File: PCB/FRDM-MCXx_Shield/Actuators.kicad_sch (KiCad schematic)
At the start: 20 parts, among them M1 Motor_Servo, U3 STPIC6C595MTR, U4 SN74LV164ADR

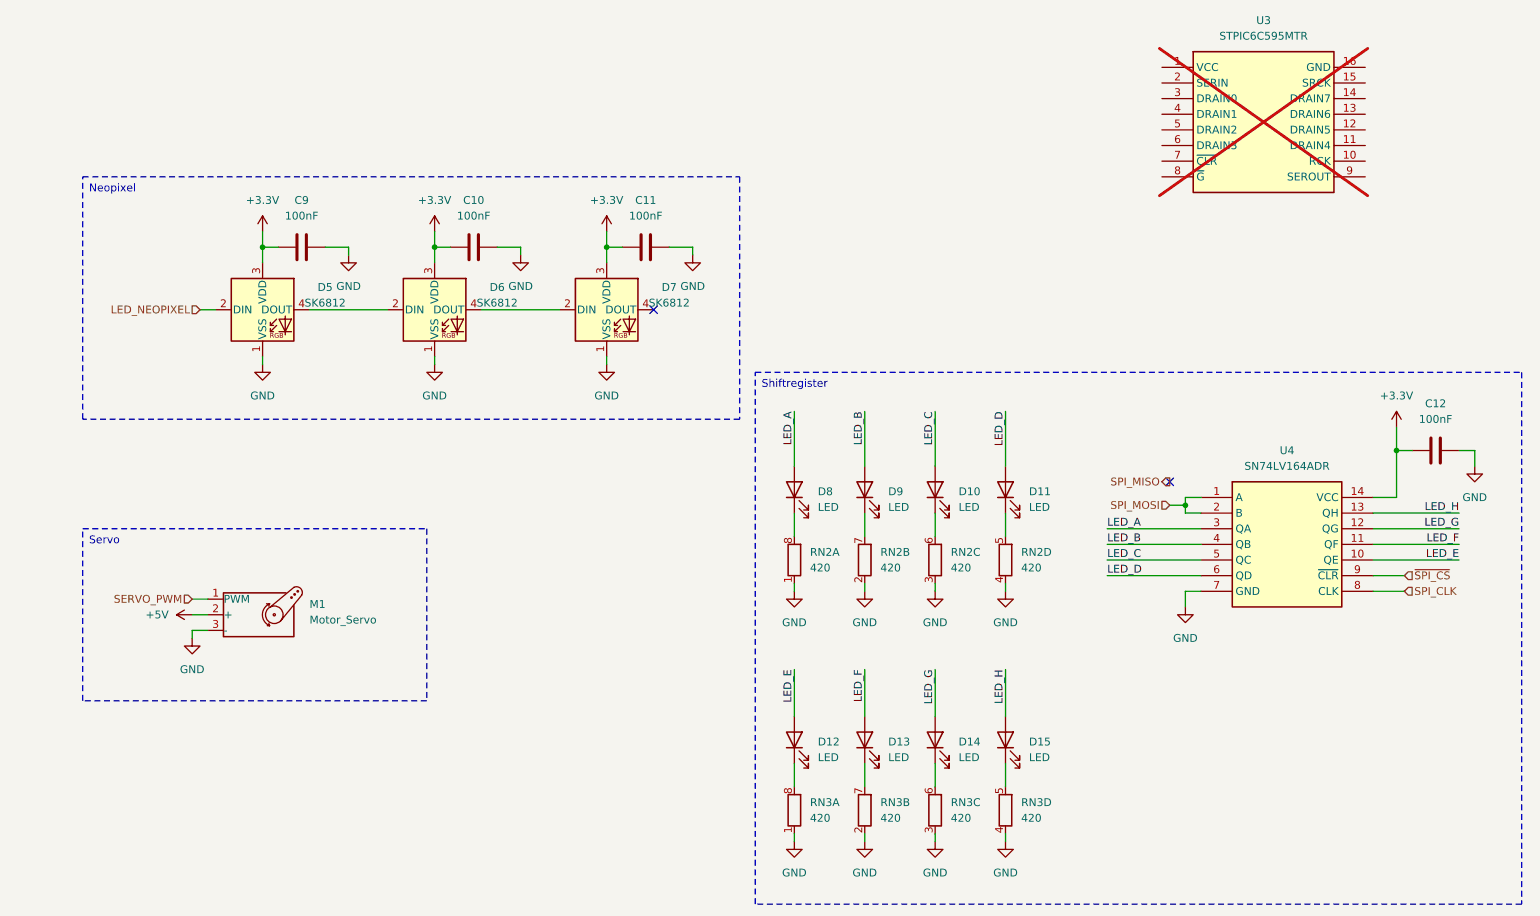
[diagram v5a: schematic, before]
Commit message: Update
Schematic: Fixed pinout, removed 5-9vin and a bunch of other stuff. Changed button/encoder debouncing.

PCB: Fixed pinout, layout and labeling. Added extra resisitors and capacitors.
Added diode direction markers.
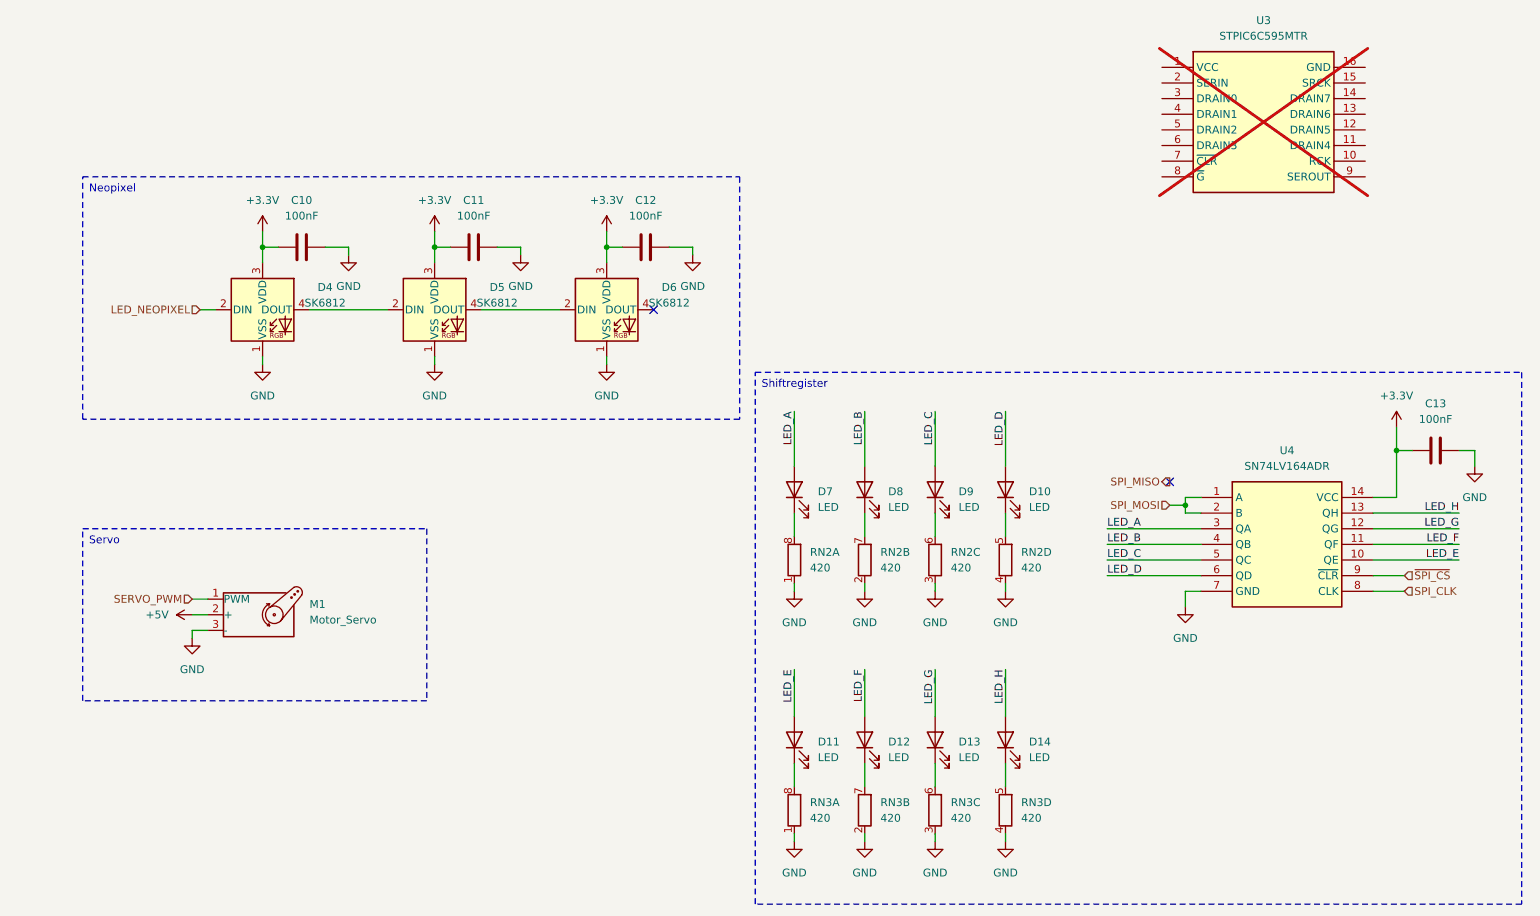
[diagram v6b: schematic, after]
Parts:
- renumbered C9 to C10, C10 to C11, C11 to C12, C12 to C13, D11 to D10, D12 to D11, D13 to D12, D14 to D13, D15 to D14, D5 to D4, D6 to D5, D7 to D6, D8 to D7, D9 to D8, D10 to D9
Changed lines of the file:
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@@
     (rev "V1.1")
     (company "HAN")
-    (comment 1 "Authors: Thomas Ijseldijk & Emiel Visser")
+    (comment 1 "Authors: Thomas Ijseldijk, Hugo Arends & Emiel Visser")
   )
   (junction (at 116.84 54.61) (diameter 0) (color 0 0 0 0)
@@
   (symbol (lib_id "Device:C") (at 251.46 87.63 90) (unit 1)
     (in_bom yes) (on_board yes) (dnp no) (fields_autoplaced)
-    (property "Reference" "C12" (at 251.46 80.01 90)
+    (property "Reference" "C13" (at 251.46 80.01 90)
       (effects (font (size 1.27 1.27)))
     )
@@
       (project "FRDM-MCXx_Shield"
         (path "/bffc27af-f9e0-4cc8-b5dc-88d2faf26a17/c2816d8d-ff46-44f3-8c3d-255f6d180fc9"
-          (reference "C12") (unit 1)
+          (reference "C13") (unit 1)
         )
       )
@@
   (symbol (lib_id "Device:LED") (at 170.18 134.62 90) (unit 1)
     (in_bom yes) (on_board yes) (dnp no) (fields_autoplaced)
-    (property "Reference" "D14" (at 173.99 134.9375 90)
+    (property "Reference" "D13" (at 173.99 134.9375 90)
       (effects (font (size 1.27 1.27)) (justify right))
     )
@@
       (project "FRDM-MCXx_Shield"
         (path "/bffc27af-f9e0-4cc8-b5dc-88d2faf26a17/c2816d8d-ff46-44f3-8c3d-255f6d180fc9"
-          (reference "D14") (unit 1)
+          (reference "D13") (unit 1)
         )
       )
@@
   (symbol (lib_id "LED:SK6812") (at 116.84 64.77 0) (unit 1)
     (in_bom yes) (on_board yes) (dnp no) (fields_autoplaced)
-    (property "Reference" "D7" (at 127 61.1221 0)
+    (property "Reference" "D6" (at 127 61.1221 0)
       (effects (font (size 1.27 1.27)))
     )
@@
       (project "FRDM-MCXx_Shield"
         (path "/bffc27af-f9e0-4cc8-b5dc-88d2faf26a17/c2816d8d-ff46-44f3-8c3d-255f6d180fc9"
-          (reference "D7") (unit 1)
+          (reference "D6") (unit 1)
         )
       )
@@
   (symbol (lib_id "Device:LED") (at 147.32 93.98 90) (unit 1)
     (in_bom yes) (on_board yes) (dnp no) (fields_autoplaced)
-    (property "Reference" "D8" (at 151.13 94.2975 90)
+    (property "Reference" "D7" (at 151.13 94.2975 90)
       (effects (font (size 1.27 1.27)) (justify right))
     )
@@
       (project "FRDM-MCXx_Shield"
         (path "/bffc27af-f9e0-4cc8-b5dc-88d2faf26a17/c2816d8d-ff46-44f3-8c3d-255f6d180fc9"
-          (reference "D8") (unit 1)
+          (reference "D7") (unit 1)
         )
       )
@@
   (symbol (lib_id "Device:LED") (at 170.18 93.98 90) (unit 1)
     (in_bom yes) (on_board yes) (dnp no) (fields_autoplaced)
-    (property "Reference" "D10" (at 173.99 94.2975 90)
+    (property "Reference" "D9" (at 173.99 94.2975 90)
       (effects (font (size 1.27 1.27)) (justify right))
     )
@@
       (project "FRDM-MCXx_Shield"
         (path "/bffc27af-f9e0-4cc8-b5dc-88d2faf26a17/c2816d8d-ff46-44f3-8c3d-255f6d180fc9"
-          (reference "D10") (unit 1)
+          (reference "D9") (unit 1)
         )
       )
@@
   (symbol (lib_id "Device:LED") (at 181.61 134.62 90) (unit 1)
     (in_bom yes) (on_board yes) (dnp no) (fields_autoplaced)
-    (property "Reference" "D15" (at 185.42 134.9375 90)
+    (property "Reference" "D14" (at 185.42 134.9375 90)
       (effects (font (size 1.27 1.27)) (justify right))
     )
@@
       (project "FRDM-MCXx_Shield"
         (path "/bffc27af-f9e0-4cc8-b5dc-88d2faf26a17/c2816d8d-ff46-44f3-8c3d-255f6d180fc9"
-          (reference "D15") (unit 1)
+          (reference "D14") (unit 1)
         )
       )
@@
   (symbol (lib_id "Device:LED") (at 158.75 134.62 90) (unit 1)
     (in_bom yes) (on_board yes) (dnp no) (fields_autoplaced)
-    (property "Reference" "D13" (at 162.56 134.9375 90)
+    (property "Reference" "D12" (at 162.56 134.9375 90)
       (effects (font (size 1.27 1.27)) (justify right))
     )
@@
       (project "FRDM-MCXx_Shield"
         (path "/bffc27af-f9e0-4cc8-b5dc-88d2faf26a17/c2816d8d-ff46-44f3-8c3d-255f6d180fc9"
-          (reference "D13") (unit 1)
+          (reference "D12") (unit 1)
         )
       )
@@
   (symbol (lib_id "Device:LED") (at 147.32 134.62 90) (unit 1)
     (in_bom yes) (on_board yes) (dnp no) (fields_autoplaced)
-    (property "Reference" "D12" (at 151.13 134.9375 90)
+    (property "Reference" "D11" (at 151.13 134.9375 90)
       (effects (font (size 1.27 1.27)) (justify right))
     )
@@
       (project "FRDM-MCXx_Shield"
         (path "/bffc27af-f9e0-4cc8-b5dc-88d2faf26a17/c2816d8d-ff46-44f3-8c3d-255f6d180fc9"
-          (reference "D12") (unit 1)
+          (reference "D11") (unit 1)
         )
       )
@@
   (symbol (lib_id "LED:SK6812") (at 60.96 64.77 0) (unit 1)
     (in_bom yes) (on_board yes) (dnp no) (fields_autoplaced)
-    (property "Reference" "D5" (at 71.12 61.1221 0)
+    (property "Reference" "D4" (at 71.12 61.1221 0)
       (effects (font (size 1.27 1.27)))
     )
@@
       (project "FRDM-MCXx_Shield"
         (path "/bffc27af-f9e0-4cc8-b5dc-88d2faf26a17/c2816d8d-ff46-44f3-8c3d-255f6d180fc9"
-          (reference "D5") (unit 1)
+          (reference "D4") (unit 1)
         )
       )
@@
   (symbol (lib_id "Device:LED") (at 158.75 93.98 90) (unit 1)
     (in_bom yes) (on_board yes) (dnp no) (fields_autoplaced)
-    (property "Reference" "D9" (at 162.56 94.2975 90)
+    (property "Reference" "D8" (at 162.56 94.2975 90)
       (effects (font (size 1.27 1.27)) (justify right))
     )
@@
       (project "FRDM-MCXx_Shield"
         (path "/bffc27af-f9e0-4cc8-b5dc-88d2faf26a17/c2816d8d-ff46-44f3-8c3d-255f6d180fc9"
-          (reference "D9") (unit 1)
+          (reference "D8") (unit 1)
         )
       )
@@
   (symbol (lib_id "Device:C") (at 123.19 54.61 90) (unit 1)
     (in_bom yes) (on_board yes) (dnp no) (fields_autoplaced)
-    (property "Reference" "C11" (at 123.19 46.99 90)
+    (property "Reference" "C12" (at 123.19 46.99 90)
       (effects (font (size 1.27 1.27)))
     )
@@
       (project "FRDM-MCXx_Shield"
         (path "/bffc27af-f9e0-4cc8-b5dc-88d2faf26a17/c2816d8d-ff46-44f3-8c3d-255f6d180fc9"
-          (reference "C11") (unit 1)
+          (reference "C12") (unit 1)
         )
       )
@@
   (symbol (lib_id "Device:LED") (at 181.61 93.98 90) (unit 1)
     (in_bom yes) (on_board yes) (dnp no) (fields_autoplaced)
-    (property "Reference" "D11" (at 185.42 94.2975 90)
+    (property "Reference" "D10" (at 185.42 94.2975 90)
       (effects (font (size 1.27 1.27)) (justify right))
     )
@@
       (project "FRDM-MCXx_Shield"
         (path "/bffc27af-f9e0-4cc8-b5dc-88d2faf26a17/c2816d8d-ff46-44f3-8c3d-255f6d180fc9"
-          (reference "D11") (unit 1)
+          (reference "D10") (unit 1)
         )
       )
@@
   (symbol (lib_id "Device:C") (at 95.25 54.61 90) (unit 1)
     (in_bom yes) (on_board yes) (dnp no) (fields_autoplaced)
-    (property "Reference" "C10" (at 95.25 46.99 90)
+    (property "Reference" "C11" (at 95.25 46.99 90)
       (effects (font (size 1.27 1.27)))
     )
@@
       (project "FRDM-MCXx_Shield"
         (path "/bffc27af-f9e0-4cc8-b5dc-88d2faf26a17/c2816d8d-ff46-44f3-8c3d-255f6d180fc9"
-          (reference "C10") (unit 1)
+          (reference "C11") (unit 1)
         )
       )
@@
   (symbol (lib_id "LED:SK6812") (at 88.9 64.77 0) (unit 1)
     (in_bom yes) (on_board yes) (dnp no) (fields_autoplaced)
-    (property "Reference" "D6" (at 99.06 61.1221 0)
+    (property "Reference" "D5" (at 99.06 61.1221 0)
       (effects (font (size 1.27 1.27)))
     )
@@
       (project "FRDM-MCXx_Shield"
         (path "/bffc27af-f9e0-4cc8-b5dc-88d2faf26a17/c2816d8d-ff46-44f3-8c3d-255f6d180fc9"
-          (reference "D6") (unit 1)
+          (reference "D5") (unit 1)
         )
       )
@@
   (symbol (lib_id "Device:C") (at 67.31 54.61 90) (unit 1)
     (in_bom yes) (on_board yes) (dnp no) (fields_autoplaced)
-    (property "Reference" "C9" (at 67.31 46.99 90)
+    (property "Reference" "C10" (at 67.31 46.99 90)
       (effects (font (size 1.27 1.27)))
     )
@@
       (project "FRDM-MCXx_Shield"
         (path "/bffc27af-f9e0-4cc8-b5dc-88d2faf26a17/c2816d8d-ff46-44f3-8c3d-255f6d180fc9"
-          (reference "C9") (unit 1)
+          (reference "C10") (unit 1)
         )
       )

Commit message: Updated footprint, PCB and schematic
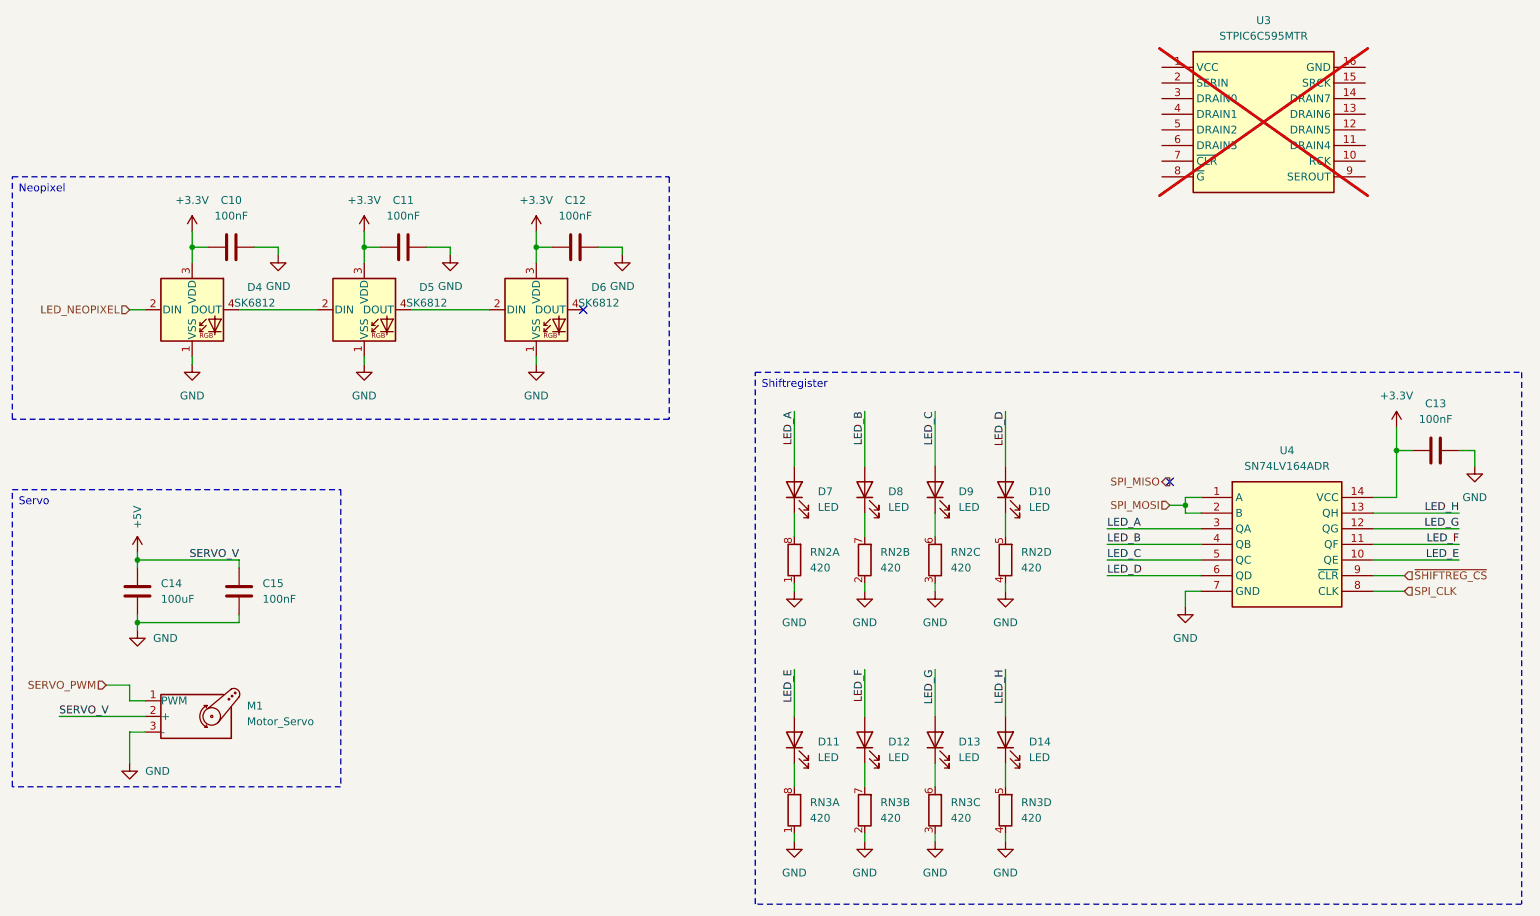
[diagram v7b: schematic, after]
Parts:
- added C14: 100uF, Capacitor_SMD:C_0603_1608Metric_Pad1.08x0.95mm_HandSolder, symbol Device:C
- added C15: 100nF, Capacitor_SMD:C_0603_1608Metric_Pad1.08x0.95mm_HandSolder, symbol Device:C
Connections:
- net +5V: now also C14.2, C15.2
- net GND: now also C14.1, C15.1
- net ~{SPI_CS} renamed ~{SHIFTREG_CS}
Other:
- moved on the sheet: C10, C11, C12, D4, D5, D6, M1
